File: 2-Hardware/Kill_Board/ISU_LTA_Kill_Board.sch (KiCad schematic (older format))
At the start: 38 parts, among them P1 CONN_2, P10 CONN_2, P11 CONN_2, P12 CONN_2, P2 CONN_2, P3 CONN_2, P4 CONN_2, P5 CONN_2, P6 CONN_2, P7 CONN_2, P8 CONN_2, P9 CONN_2, Q1 NMOS+PMOS, Q2 N-CH, Q3 N-CH, U1 LM2937, U2 74LVC1G374

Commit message: Work on new Rev. E board
Initial start on Rev. E Board.
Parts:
- added D?: LED, symbol LED
- C1, C2, C3, C4: symbol C -> C-RESCUE-ISU_LTA_Kill_Board
- D1, D2: symbol LED -> LED-RESCUE-ISU_LTA_Kill_Board
- Q2, Q3: symbol MOS_3-TERM -> MOS_3-Term
- R1, R10, R11, R2, R3, R4, R5, R6, R7, R8, R9: symbol R -> R-RESCUE-ISU_LTA_Kill_Board
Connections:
- wire segments 137 -> 88

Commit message: Start of moving to Feather board
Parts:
- removed C1: 0.1uF, symbol C-RESCUE-ISU_LTA_Kill_Board
- removed C5: 0.1uF, symbol C-SPLIT
- removed D?: LED, symbol LED
- removed XB1: XBEE, symbol XBEE
- added U?: Feather32u4RFM95, symbol Feather32u4RFM95
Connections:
- wire segments 88 -> 82
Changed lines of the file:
@@
 	10200 6050 10200 3600
 Wire Wire Line
-	2000 3600 10200 3600
+	10200 3600 2000 3600
 Connection ~ 2000 3600
 Wire Wire Line
@@
 Wire Wire Line
 	7950 1650 8750 1650
-Wire Wire Line
-	5350 1750 5500 1750
-Wire Wire Line
-	5550 2650 5550 2750
 Connection ~ 7050 5200
 Wire Wire Line
@@
 	5900 1800 5900 1650
 Wire Wire Line
-	5350 1650 6750 1650
-Wire Wire Line
 	7350 2100 7350 2000
 Wire Wire Line
@@
 Wire Wire Line
 	10050 5200 10050 4950
-Connection ~ 2800 1650
-Wire Wire Line
-	2800 1500 2800 1900
-Wire Wire Line
-	3250 2550 2800 2550
 Wire Wire Line
 	3150 4400 3100 4400
@@
 	6000 6150 5800 6150
 Wire Wire Line
-	5800 5200 5800 6150
+	5800 6150 5800 5200
 Wire Wire Line
 	7350 4950 7350 5100
@@
 Wire Wire Line
 	4000 4400 4000 4350
-Wire Wire Line
-	3250 1650 2800 1650
-Wire Wire Line
-	2800 2300 2800 2750
-Connection ~ 2800 2550
 Wire Wire Line
 	9850 5100 9850 4950
@@
 	5200 5200 5200 5100
 Wire Wire Line
-	5500 2250 5350 2250
-Wire Wire Line
-	5600 2250 5600 2200
-Wire Wire Line
 	3550 4700 3550 5250
 Wire Wire Line
 	2900 4000 3200 4000
 Connection ~ 3100 4000
-$Comp
-L C-SPLIT C5
-U 1 1 509F1F26
-P 5550 2450
-F 0 "C5" H 5600 2550 50  0000 L CNN
-F 1 "0.1uF" H 5600 2350 50  0000 L CNN
-F 2 "" H 5550 2450 60  0001 C CNN
-F 3 "" H 5550 2450 60  0001 C CNN
-F 4 "311-1141-1-ND" H 5550 2450 60  0001 C CNN "DigikeyNumber"
-F 5 "Yageo" H 5550 2450 60  0001 C CNN "Manufacturer"
-F 6 "CC0805KRX7R8BB104" H 5550 2450 60  0001 C CNN "ManufacturerNumber"
-F 7 "1" H 5550 2450 60  0001 C CNN "Qty"
-	1    5550 2450
-	1    0    0    -1
-$EndComp
 $Comp
 L R-RESCUE-ISU_LTA_Kill_Board R11
@@
 F 7 "1" H 5100 4300 60  0001 C CNN "Qty"
 	1    5100 4300
-	1    0    0    -1
-$EndComp
-$Comp
-L XBEE XB1
-U 1 1 50778DA5
-P 4300 2100
-F 0 "XB1" H 4300 2900 60  0000 C CNN
-F 1 "XBEE" H 4300 3000 60  0000 C CNN
-F 2 "" H 4300 2100 60  0001 C CNN
-F 3 "" H 4300 2100 60  0001 C CNN
-F 4 "S5751-10-ND" H 4300 2100 60  0001 C CNN "DigikeyNumber"
-F 5 "Sullins Connector Solutions" H 4300 2100 60  0001 C CNN "Manufacturer"
-F 6 "NPPN101BFCN-RC" H 4300 2100 60  0001 C CNN "ManufacturerNumber"
-F 7 "2" H 4300 2100 60  0001 C CNN "Qty"
-	1    4300 2100
 	1    0    0    -1
 $EndComp
@@
 Text Label 4600 4600 2    60   ~ 0
 Ctrl
-Text Label 5500 1750 0    60   ~ 0
+Text Label 3300 1650 2    60   ~ 0
 V_Sense
 Text Label 2750 4600 2    60   ~ 0
@@
 F 7 "1" H 4000 4600 60  0001 C CNN "Qty"
 	1    4000 4600
-	1    0    0    -1
-$EndComp
-$Comp
-L GND-RESCUE-ISU_LTA_Kill_Board #PWR01
-U 1 1 5071CBC9
-P 5550 2750
-F 0 "#PWR01" H 5550 2750 30  0001 C CNN
-F 1 "GND" H 5550 2680 30  0001 C CNN
-F 2 "" H 5550 2750 60  0001 C CNN
-F 3 "" H 5550 2750 60  0001 C CNN
-	1    5550 2750
 	1    0    0    -1
 $EndComp
@@
 $EndComp
 $Comp
-L +3.3V-RESCUE-ISU_LTA_Kill_Board #PWR07
-U 1 1 50666BB7
-P 5600 2200
-F 0 "#PWR07" H 5600 2160 30  0001 C CNN
-F 1 "+3.3V" H 5600 2310 30  0000 C CNN
-F 2 "" H 5600 2200 60  0001 C CNN
-F 3 "" H 5600 2200 60  0001 C CNN
-	1    5600 2200
-	1    0    0    -1
-$EndComp
-$Comp
 L CONN_2 P12
 U 1 1 50666ACA
@@
 $EndComp
 $Comp
-L C-RESCUE-ISU_LTA_Kill_Board C1
-U 1 1 505D3F6B
-P 2800 2100
-F 0 "C1" H 2850 2200 50  0000 L CNN
-F 1 "0.1uF" H 2850 2000 50  0000 L CNN
-F 2 "" H 2800 2100 60  0001 C CNN
-F 3 "" H 2800 2100 60  0001 C CNN
-F 4 "311-1141-1-ND" H 2800 2100 60  0001 C CNN "DigikeyNumber"
-F 5 "Yageo" H 2800 2100 60  0001 C CNN "Manufacturer"
-F 6 "CC0805KRX7R8BB104" H 2800 2100 60  0001 C CNN "ManufacturerNumber"
-F 7 "1" H 2800 2100 60  0001 C CNN "Qty"
-	1    2800 2100
-	1    0    0    -1
-$EndComp
-$Comp
 L GND-RESCUE-ISU_LTA_Kill_Board #PWR08
 U 1 1 505D3F53
-P 2800 2750
-F 0 "#PWR08" H 2800 2750 30  0001 C CNN
-F 1 "GND" H 2800 2680 30  0001 C CNN
-F 2 "" H 2800 2750 60  0001 C CNN
-F 3 "" H 2800 2750 60  0001 C CNN
-	1    2800 2750
-	1    0    0    -1
-$EndComp
-$Comp
-L +3.3V-RESCUE-ISU_LTA_Kill_Board #PWR09
-U 1 1 505D3F4E
-P 2800 1500
-F 0 "#PWR09" H 2800 1460 30  0001 C CNN
-F 1 "+3.3V" H 2800 1610 30  0000 C CNN
-F 2 "" H 2800 1500 60  0001 C CNN
-F 3 "" H 2800 1500 60  0001 C CNN
-	1    2800 1500
-	1    0    0    -1
+P 3150 1300
+F 0 "#PWR08" H 3150 1300 30  0001 C CNN
+F 1 "GND" H 3150 1230 30  0001 C CNN
+F 2 "" H 3150 1300 60  0001 C CNN
+F 3 "" H 3150 1300 60  0001 C CNN
+	1    3150 1300
+	0    1    1    0
 $EndComp
 $Comp
@@
 $EndComp
 $Comp
-L LED D?
-U 1 1 577EC6FB
-P 9750 2950
-F 0 "D?" H 9750 3050 50  0000 C CNN
-F 1 "LED" H 9750 2850 50  0000 C CNN
-F 2 "" H 9750 2950 50  0000 C CNN
-F 3 "" H 9750 2950 50  0000 C CNN
-	1    9750 2950
-	1    0    0    -1
-$EndComp
+L Feather32u4RFM95 U?
+U 1 1 581975B1
+P 4350 1950
+F 0 "U?" H 4350 1950 60  0000 C CNN
+F 1 "Feather32u4RFM95" H 4350 1950 79  0000 C CNN
+F 2 "" H 4350 1950 60  0001 C CNN
+F 3 "" H 4350 1950 60  0001 C CNN
+	1    4350 1950
+	0    1    1    0
+$EndComp
+Wire Wire Line
+	3550 1300 3150 1300
+Wire Wire Line
+	5150 1650 6750 1650
+Wire Wire Line
+	3550 1650 3300 1650
 $EndSCHEMATC

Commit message: Update to schematic with new feather part
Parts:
- removed U?: Feather32u4RFM95, symbol Feather32u4RFM95
- added P1, P2, P3: CONN_01X02, symbol CONN_01X02
- added P4, P5, P6: CONN_01X03, symbol CONN_01X03
- added U1: ADAFRUIT_FEATHER, symbol ADAFRUIT_FEATHER
- renumbered C2 to C1, C3 to C2, C4 to C3, P4 to P10, P5 to P11, P6 to P12, P7 to P13, P8 to P14, P9 to P15, P10 to P16, P11 to P17, P12 to P18, P1 to P7, P2 to P8, P3 to P9, R9 to R1, R7 to R10, R8 to R11, R10 to R2, R2 to R3, R3 to R4, R11 to R5, R5 to R6, R6 to R7, R1 to R8, R4 to R9, U1 to U2, U2 to U3
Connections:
- wire segments 82 -> 112
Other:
- moved on the sheet: C3, D2, R10, R11, R9, U3

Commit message: minor update
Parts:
- P1, P2, P3: footprint (none) -> Connect:PINHEAD1-2
- P4, P5, P6: footprint (none) -> Connect:PINHEAD1-3
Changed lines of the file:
@@
 F 0 "P1" H 3850 850 50  0000 C CNN
 F 1 "CONN_01X02" V 3950 700 50  0000 C CNN
-F 2 "" H 3850 700 50  0000 C CNN
+F 2 "Connect:PINHEAD1-2" H 3850 700 50  0001 C CNN
 F 3 "" H 3850 700 50  0000 C CNN
 	1    3850 700
@@
 F 0 "P2" H 4400 850 50  0000 C CNN
 F 1 "CONN_01X02" V 4500 700 50  0000 C CNN
-F 2 "" H 4400 700 50  0000 C CNN
+F 2 "Connect:PINHEAD1-2" H 4400 700 50  0001 C CNN
 F 3 "" H 4400 700 50  0000 C CNN
 	1    4400 700
@@
 F 0 "P3" H 4950 850 50  0000 C CNN
 F 1 "CONN_01X02" V 5050 700 50  0000 C CNN
-F 2 "" H 4950 700 50  0000 C CNN
+F 2 "Connect:PINHEAD1-2" H 4950 700 50  0001 C CNN
 F 3 "" H 4950 700 50  0000 C CNN
 	1    4950 700
@@
 F 0 "P4" H 5550 900 50  0000 C CNN
 F 1 "CONN_01X03" V 5650 700 50  0000 C CNN
-F 2 "" H 5550 700 50  0000 C CNN
+F 2 "Connect:PINHEAD1-3" H 5550 700 50  0001 C CNN
 F 3 "" H 5550 700 50  0000 C CNN
 	1    5550 700
@@
 F 0 "P5" H 6100 900 50  0000 C CNN
 F 1 "CONN_01X03" V 6200 700 50  0000 C CNN
-F 2 "" H 6100 700 50  0000 C CNN
+F 2 "Connect:PINHEAD1-3" H 6100 700 50  0001 C CNN
 F 3 "" H 6100 700 50  0000 C CNN
 	1    6100 700
@@
 F 0 "P6" H 6650 900 50  0000 C CNN
 F 1 "CONN_01X03" V 6750 700 50  0000 C CNN
-F 2 "" H 6650 700 50  0000 C CNN
+F 2 "Connect:PINHEAD1-3" H 6650 700 50  0001 C CNN
 F 3 "" H 6650 700 50  0000 C CNN
 	1    6650 700

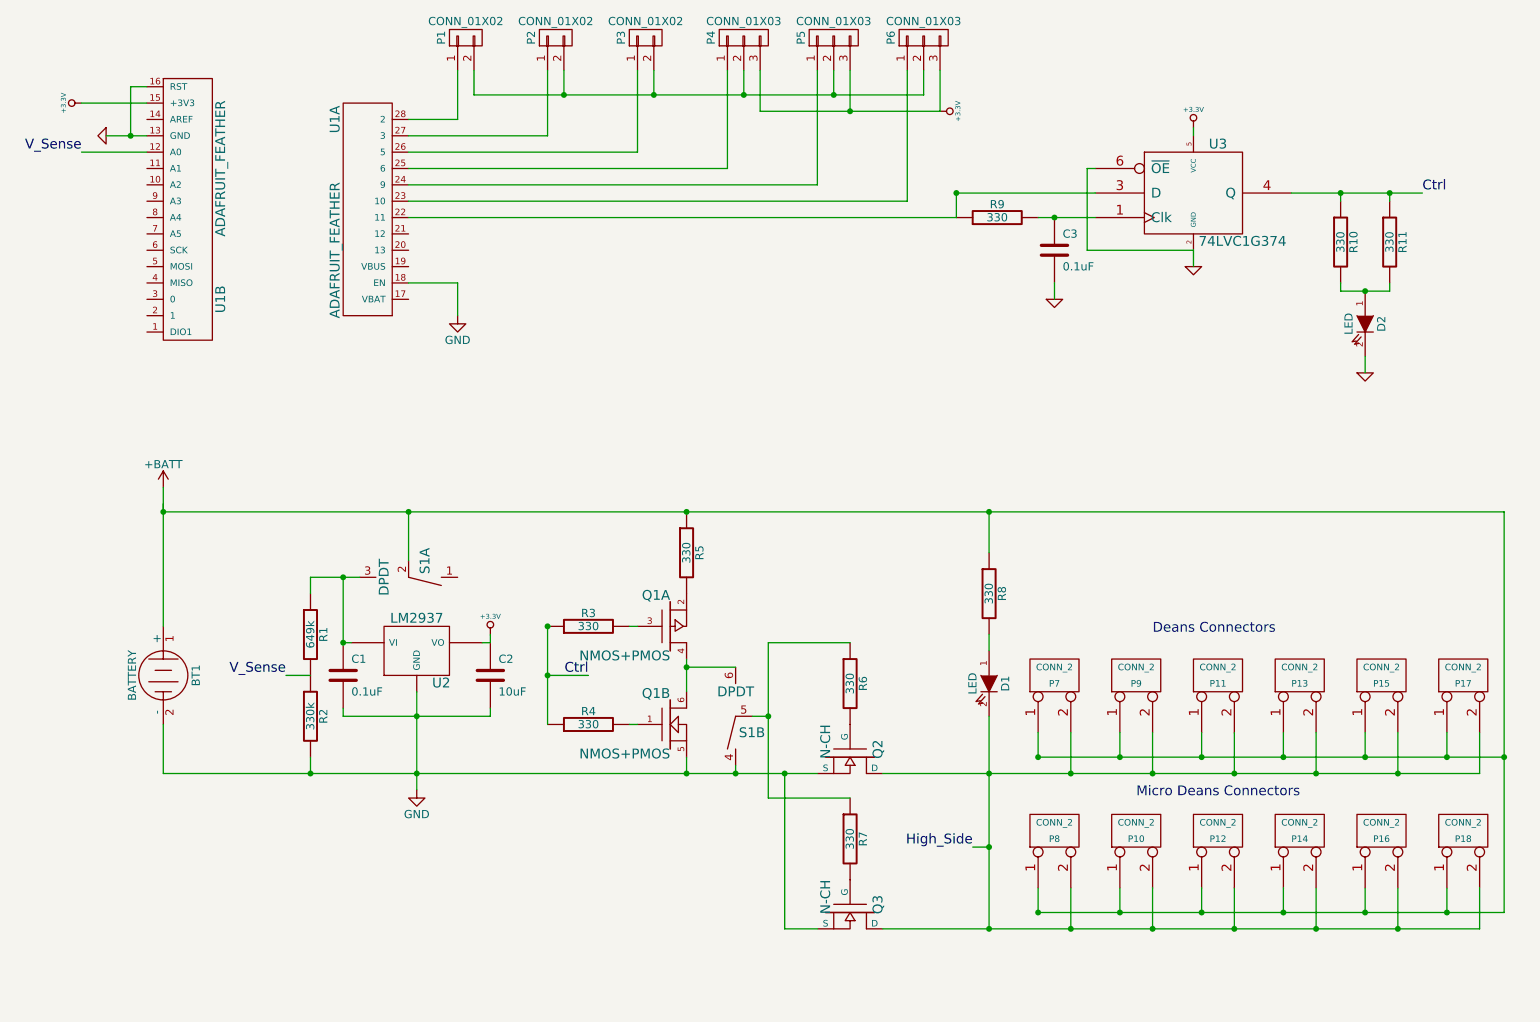
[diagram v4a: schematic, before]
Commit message: Circuit clean up
Removed flip flop (not needed).  Moved a connector off pin 9 since it
is tied to monitor internal battery.  Right now, board is powered from
on board reg and not the feather reg.  Disabled feather regulator
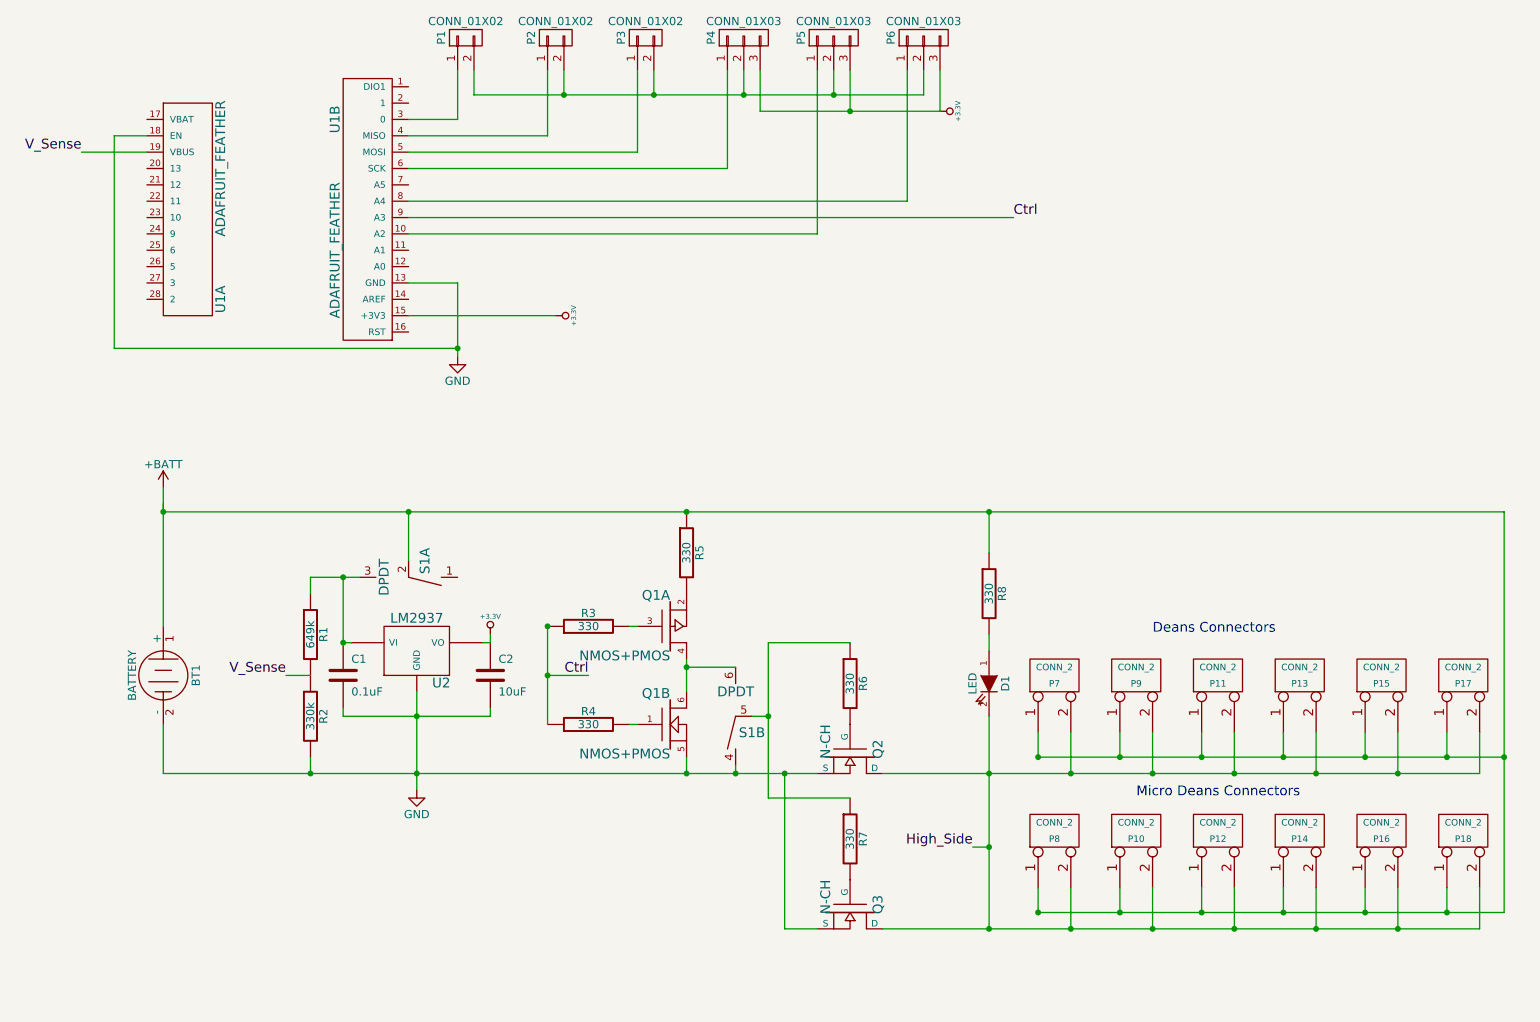
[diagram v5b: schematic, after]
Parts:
- removed C3: 0.1uF, symbol C-RESCUE-ISU_LTA_Kill_Board
- removed D2: LED, symbol LED-RESCUE-ISU_LTA_Kill_Board
- removed R10, R11, R9: 330, symbol R-RESCUE-ISU_LTA_Kill_Board
- removed U3: 74LVC1G374, symbol 74LVC1G374
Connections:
- net +3.3V: now also U1.15 (+3V3); no longer U1.15 (+3V3)
- net Ctrl: now also U1.9 (A3)
- net GND: now also U1.13 (GND), U1.18 (EN); no longer U1.13 (GND), U1.16 (RST), U1.18 (EN)
- net V_Sense: now also U1.19 (VBUS); no longer U1.12 (A0)
- net at P6.1 (P1): now also U1.8 (A4); no longer U1.23 (10)
- net at P5.1 (P1): now also U1.10 (A2); no longer U1.24 (9)
- net at P4.1 (P1): now also U1.6 (SCK); no longer U1.25 (6)
- net at P3.1 (P1): now also U1.5 (MOSI); no longer U1.26 (5)
- net at P2.1 (P1): now also U1.4 (MISO); no longer U1.27 (3)
- net at P1.1 (P1): now also U1.3 (0); no longer U1.28 (2)

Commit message: Updates to modules
Updated to mapping parts to modules
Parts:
- BT1, P11, P13, P15, P17, P7, P9: footprint (none) -> Connectors:DEANS
- D1: footprint (none) -> LEDs:LED_0805
- P1, P2, P3: footprint Connect:PINHEAD1-2 -> Connectors_Ian:CONN_2.54mm_1x2
- P10, P12, P14, P16, P18, P8: footprint (none) -> Connectors:DEANS_MICRO
- P4, P5, P6: footprint Connect:PINHEAD1-3 -> Connectors_Ian:CONN_2.54mm_1x3
- Q1: footprint (none) -> SMD:SOT-23-6
- Q2, Q3: footprint (none) -> TO_SOT_Packages_SMD:SOT-404
- S1: footprint (none) -> Switches:DPDT_ESWITCH_EG2207
- U1: footprint (none) -> Modules_Ian:ADAFRUIT_FEATHER
- U2: footprint (none) -> TO_SOT_Packages_SMD:SOT-223
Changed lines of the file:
@@
 F 0 "Q1" H 5100 5090 60  0000 R CNN
 F 1 "NMOS+PMOS" H 5100 4720 60  0000 R CNN
-F 2 "" H 5100 4900 60  0001 C CNN
+F 2 "SMD:SOT-23-6" H 5100 4900 60  0001 C CNN
 F 3 "" H 5100 4900 60  0001 C CNN
 F 4 "FDC6333CCT-ND" H 5100 4900 60  0001 C CNN "DigikeyNumber"
@@
 F 0 "Q1" H 5100 4490 60  0000 R CNN
 F 1 "NMOS+PMOS" H 5100 4120 60  0000 R CNN
-F 2 "" H 5100 4300 60  0001 C CNN
+F 2 "SMD:SOT-23-6" H 5100 4300 60  0001 C CNN
 F 3 "" H 5100 4300 60  0001 C CNN
 F 4 "FDC6333CCT-ND" H 5100 4300 60  0001 C CNN "DigikeyNumber"
@@
 F 0 "Q2" H 6210 5270 60  0000 R CNN
 F 1 "N-CH" H 6210 4950 60  0000 R CNN
-F 2 "" H 6200 5100 60  0001 C CNN
+F 2 "TO_SOT_Packages_SMD:SOT-404" H 6200 5100 60  0001 C CNN
 F 3 "" H 6200 5100 60  0001 C CNN
 F 4 "568-6587-1-ND" H 6200 5100 60  0001 C CNN "DigikeyNumber"
@@
 F 0 "Q3" H 6210 6220 60  0000 R CNN
 F 1 "N-CH" H 6210 5900 60  0000 R CNN
-F 2 "" H 6200 6050 60  0001 C CNN
+F 2 "TO_SOT_Packages_SMD:SOT-404" H 6200 6050 60  0001 C CNN
 F 3 "" H 6200 6050 60  0001 C CNN
 F 4 "568-6587-1-ND" H 6200 6050 60  0001 C CNN "DigikeyNumber"
@@
 F 0 "U2" H 3700 4254 60  0000 C CNN
 F 1 "LM2937" H 3550 4650 60  0000 C CNN
-F 2 "" H 3550 4450 60  0001 C CNN
+F 2 "TO_SOT_Packages_SMD:SOT-223" H 3550 4450 60  0001 C CNN
 F 3 "" H 3550 4450 60  0001 C CNN
 F 4 "LM2937IMP-3.3/NOPBCT-ND" H 3550 4450 60  0001 C CNN "DigikeyNumber"
@@
 F 0 "S1" H 5600 4750 60  0000 C CNN
 F 1 "DPDT" H 5500 5000 60  0000 C CNN
-F 2 "" H 5500 4850 60  0001 C CNN
+F 2 "Switches:DPDT_ESWITCH_EG2207" H 5500 4850 60  0001 C CNN
 F 3 "" H 5500 4850 60  0001 C CNN
 F 4 "EG1940-ND" H 5500 4850 60  0001 C CNN "DigikeyNumber"
@@
 F 0 "S1" H 3600 3900 60  0000 C CNN
 F 1 "DPDT" H 3500 4150 60  0000 C CNN
-F 2 "" H 3500 4000 60  0001 C CNN
+F 2 "Switches:DPDT_ESWITCH_EG2207" H 3500 4000 60  0001 C CNN
 F 3 "" H 3500 4000 60  0001 C CNN
 F 4 "EG1940-ND" H 3500 4000 60  0001 C CNN "DigikeyNumber"
@@
 F 0 "D1" H 7050 4750 50  0000 C CNN
 F 1 "LED" H 7050 4550 50  0000 C CNN
-F 2 "" H 7050 4650 60  0001 C CNN
+F 2 "LEDs:LED_0805" H 7050 4650 60  0001 C CNN
 F 3 "" H 7050 4650 60  0001 C CNN
 F 4 "754-1141-1-ND" H 7050 4650 60  0001 C CNN "DigikeyNumber"
@@
 F 0 "P18" V 9900 5550 40  0000 C CNN
 F 1 "CONN_2" V 10000 5550 40  0000 C CNN
-F 2 "" H 9950 5550 60  0001 C CNN
+F 2 "Connectors:DEANS_MICRO" H 9950 5550 60  0001 C CNN
 F 3 "" H 9950 5550 60  0001 C CNN
 	1    9950 5550
@@
 F 0 "P17" V 9900 4600 40  0000 C CNN
 F 1 "CONN_2" V 10000 4600 40  0000 C CNN
-F 2 "" H 9950 4600 60  0001 C CNN
+F 2 "Connectors:DEANS" H 9950 4600 60  0001 C CNN
 F 3 "" H 9950 4600 60  0001 C CNN
 	1    9950 4600
@@
 F 0 "P8" V 7400 5550 40  0000 C CNN
 F 1 "CONN_2" V 7500 5550 40  0000 C CNN
-F 2 "" H 7450 5550 60  0001 C CNN
+F 2 "Connectors:DEANS_MICRO" H 7450 5550 60  0001 C CNN
 F 3 "" H 7450 5550 60  0001 C CNN
 	1    7450 5550
@@
 F 0 "P10" V 7900 5550 40  0000 C CNN
 F 1 "CONN_2" V 8000 5550 40  0000 C CNN
-F 2 "" H 7950 5550 60  0001 C CNN
+F 2 "Connectors:DEANS_MICRO" H 7950 5550 60  0001 C CNN
 F 3 "" H 7950 5550 60  0001 C CNN
 	1    7950 5550
@@
 F 0 "P12" V 8400 5550 40  0000 C CNN
 F 1 "CONN_2" V 8500 5550 40  0000 C CNN
-F 2 "" H 8450 5550 60  0001 C CNN
+F 2 "Connectors:DEANS_MICRO" H 8450 5550 60  0001 C CNN
 F 3 "" H 8450 5550 60  0001 C CNN
 	1    8450 5550
@@
 F 0 "P14" V 8900 5550 40  0000 C CNN
 F 1 "CONN_2" V 9000 5550 40  0000 C CNN
-F 2 "" H 8950 5550 60  0001 C CNN
+F 2 "Connectors:DEANS_MICRO" H 8950 5550 60  0001 C CNN
 F 3 "" H 8950 5550 60  0001 C CNN
 	1    8950 5550
@@
 F 0 "P16" V 9400 5550 40  0000 C CNN
 F 1 "CONN_2" V 9500 5550 40  0000 C CNN
-F 2 "" H 9450 5550 60  0001 C CNN
+F 2 "Connectors:DEANS_MICRO" H 9450 5550 60  0001 C CNN
 F 3 "" H 9450 5550 60  0001 C CNN
 	1    9450 5550
@@
 F 0 "P15" V 9400 4600 40  0000 C CNN
 F 1 "CONN_2" V 9500 4600 40  0000 C CNN
-F 2 "" H 9450 4600 60  0001 C CNN
+F 2 "Connectors:DEANS" H 9450 4600 60  0001 C CNN
 F 3 "" H 9450 4600 60  0001 C CNN
 	1    9450 4600
@@
 F 0 "P13" V 8900 4600 40  0000 C CNN
 F 1 "CONN_2" V 9000 4600 40  0000 C CNN
-F 2 "" H 8950 4600 60  0001 C CNN
+F 2 "Connectors:DEANS" H 8950 4600 60  0001 C CNN
 F 3 "" H 8950 4600 60  0001 C CNN
 	1    8950 4600
@@
 F 0 "P11" V 8400 4600 40  0000 C CNN
 F 1 "CONN_2" V 8500 4600 40  0000 C CNN
-F 2 "" H 8450 4600 60  0001 C CNN
+F 2 "Connectors:DEANS" H 8450 4600 60  0001 C CNN
 F 3 "" H 8450 4600 60  0001 C CNN
 	1    8450 4600
@@
 F 0 "P9" V 7900 4600 40  0000 C CNN
 F 1 "CONN_2" V 8000 4600 40  0000 C CNN
-F 2 "" H 7950 4600 60  0001 C CNN
+F 2 "Connectors:DEANS" H 7950 4600 60  0001 C CNN
 F 3 "" H 7950 4600 60  0001 C CNN
 	1    7950 4600
@@
 F 0 "P7" V 7400 4600 40  0000 C CNN
 F 1 "CONN_2" V 7500 4600 40  0000 C CNN
-F 2 "" H 7450 4600 60  0001 C CNN
+F 2 "Connectors:DEANS" H 7450 4600 60  0001 C CNN
 F 3 "" H 7450 4600 60  0001 C CNN
 	1    7450 4600
@@
 F 0 "BT1" H 2000 4800 50  0000 C CNN
 F 1 "BATTERY" H 2000 4410 50  0000 C CNN
-F 2 "" H 2000 4600 60  0001 C CNN
+F 2 "Connectors:DEANS" H 2000 4600 60  0001 C CNN
 F 3 "" H 2000 4600 60  0001 C CNN
 	1    2000 4600
@@
 F 0 "U1" V 2350 1200 60  0000 C CNN
 F 1 "ADAFRUIT_FEATHER" V 2350 2000 60  0000 C CNN
-F 2 "" H 2300 1550 60  0000 C CNN
+F 2 "Modules_Ian:ADAFRUIT_FEATHER" H 2300 1550 60  0001 C CNN
 F 3 "" H 2300 1550 60  0000 C CNN
 	1    2150 1750
@@
 F 0 "U1" V 3450 1200 60  0000 C CNN
 F 1 "ADAFRUIT_FEATHER" V 3450 2000 60  0000 C CNN
-F 2 "" H 3400 1550 60  0000 C CNN
+F 2 "Modules_Ian:ADAFRUIT_FEATHER" H 3400 1550 60  0001 C CNN
 F 3 "" H 3400 1550 60  0000 C CNN
 	2    3250 1750
@@
 F 0 "P1" H 3850 850 50  0000 C CNN
 F 1 "CONN_01X02" V 3950 700 50  0000 C CNN
-F 2 "Connect:PINHEAD1-2" H 3850 700 50  0001 C CNN
+F 2 "Connectors_Ian:CONN_2.54mm_1x2" H 3850 700 50  0001 C CNN
 F 3 "" H 3850 700 50  0000 C CNN
 	1    3850 700
@@
 F 0 "P2" H 4400 850 50  0000 C CNN
 F 1 "CONN_01X02" V 4500 700 50  0000 C CNN
-F 2 "Connect:PINHEAD1-2" H 4400 700 50  0001 C CNN
+F 2 "Connectors_Ian:CONN_2.54mm_1x2" H 4400 700 50  0001 C CNN
 F 3 "" H 4400 700 50  0000 C CNN
 	1    4400 700
@@
 F 0 "P3" H 4950 850 50  0000 C CNN
 F 1 "CONN_01X02" V 5050 700 50  0000 C CNN
-F 2 "Connect:PINHEAD1-2" H 4950 700 50  0001 C CNN
+F 2 "Connectors_Ian:CONN_2.54mm_1x2" H 4950 700 50  0001 C CNN
 F 3 "" H 4950 700 50  0000 C CNN
 	1    4950 700
@@
 F 0 "P4" H 5550 900 50  0000 C CNN
 F 1 "CONN_01X03" V 5650 700 50  0000 C CNN
-F 2 "Connect:PINHEAD1-3" H 5550 700 50  0001 C CNN
+F 2 "Connectors_Ian:CONN_2.54mm_1x3" H 5550 700 50  0001 C CNN
 F 3 "" H 5550 700 50  0000 C CNN
 	1    5550 700
@@
 F 0 "P5" H 6100 900 50  0000 C CNN
 F 1 "CONN_01X03" V 6200 700 50  0000 C CNN
-F 2 "Connect:PINHEAD1-3" H 6100 700 50  0001 C CNN
+F 2 "Connectors_Ian:CONN_2.54mm_1x3" H 6100 700 50  0001 C CNN
 F 3 "" H 6100 700 50  0000 C CNN
 	1    6100 700
@@
 F 0 "P6" H 6650 900 50  0000 C CNN
 F 1 "CONN_01X03" V 6750 700 50  0000 C CNN
-F 2 "Connect:PINHEAD1-3" H 6650 700 50  0001 C CNN
+F 2 "Connectors_Ian:CONN_2.54mm_1x3" H 6650 700 50  0001 C CNN
 F 3 "" H 6650 700 50  0000 C CNN
 	1    6650 700
